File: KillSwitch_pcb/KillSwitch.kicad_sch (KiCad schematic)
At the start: 27 parts, among them IC1 Wio-SX1262, J1 J_ESP_DBG_UART, J2 USB_C_Receptacle_USB2.0, SW1 SW_DIP_x08, SW2 SW_RESET, SW3 SW_BOOT, SW4 ARM, U1 ESP32-S3-WROOM-1

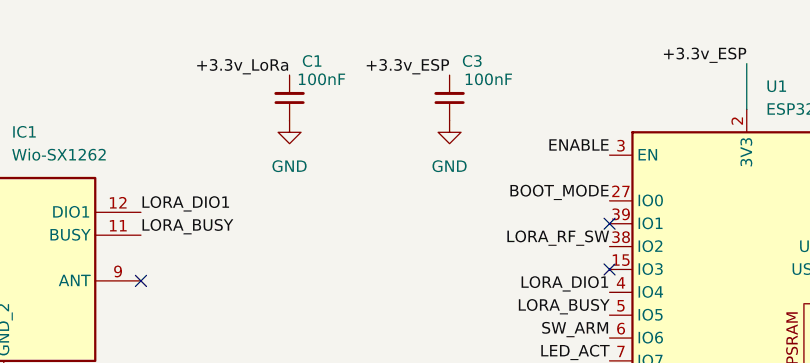
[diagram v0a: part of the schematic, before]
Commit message: replace 100nF caps with 470nf
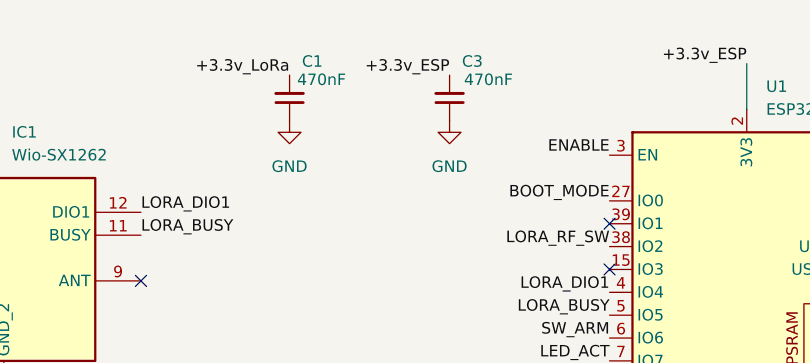
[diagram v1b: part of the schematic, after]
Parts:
- C1, C3: value 100nF -> 470nF
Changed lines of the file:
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@@
 			)
 		)
-		(property "Value" "100nF"
+		(property "Value" "470nF"
 			(at 93.726 23.368 0)
 			(effects
@@
 			)
 		)
-		(property "Value" "100nF"
+		(property "Value" "470nF"
 			(at 112.268 23.368 0)
 			(effects
